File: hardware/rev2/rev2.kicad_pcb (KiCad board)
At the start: 2 copper layers, 83.8 x 94 mm, 44 parts, among them J1 Conn_01x09_Female, J2 RFM9X_header, J3 Conn_01x03_Male, Q1 Q_PNP_BCE, U1 BNO055, U2 MPL3115A2, U3 Teensy3.6, U4 BMI088, U5 ADXL345BCCZ, Y1 Crystal_32kHz768

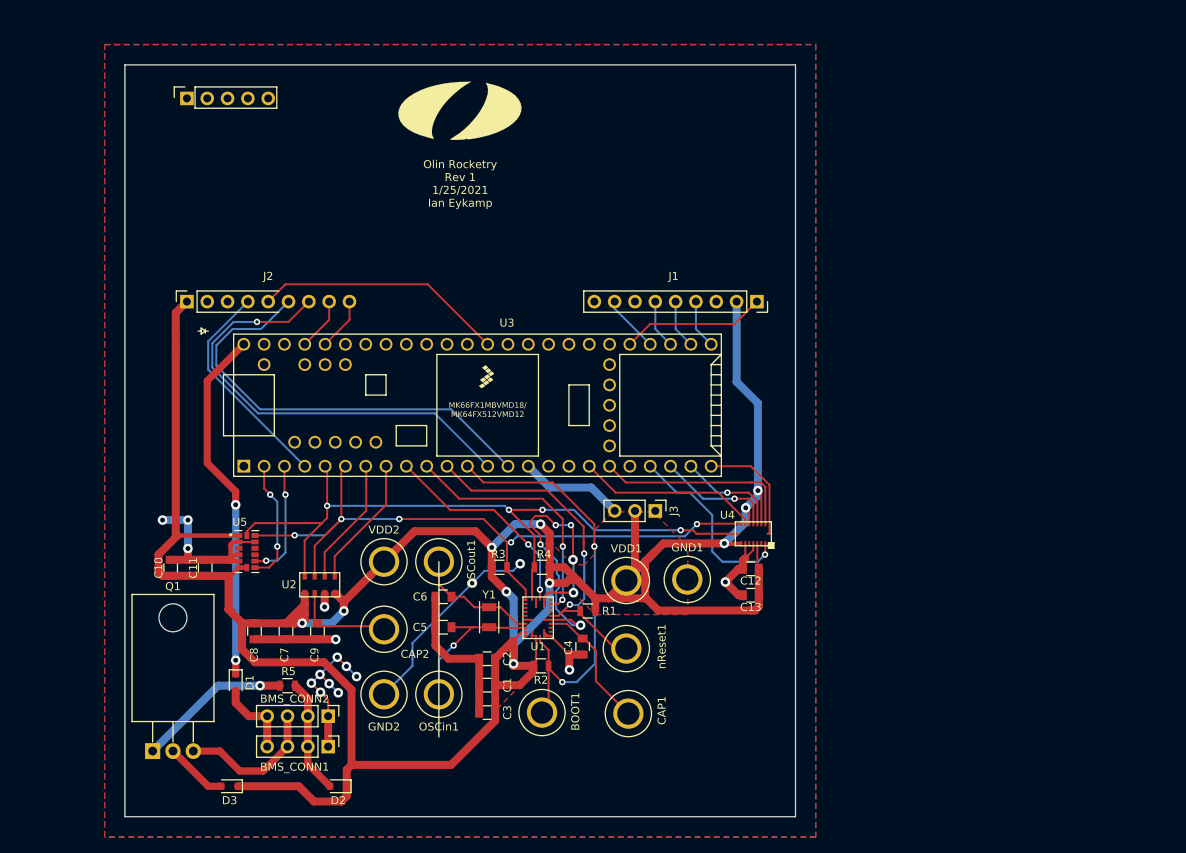
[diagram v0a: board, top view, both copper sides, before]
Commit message: remove extra traces from layout
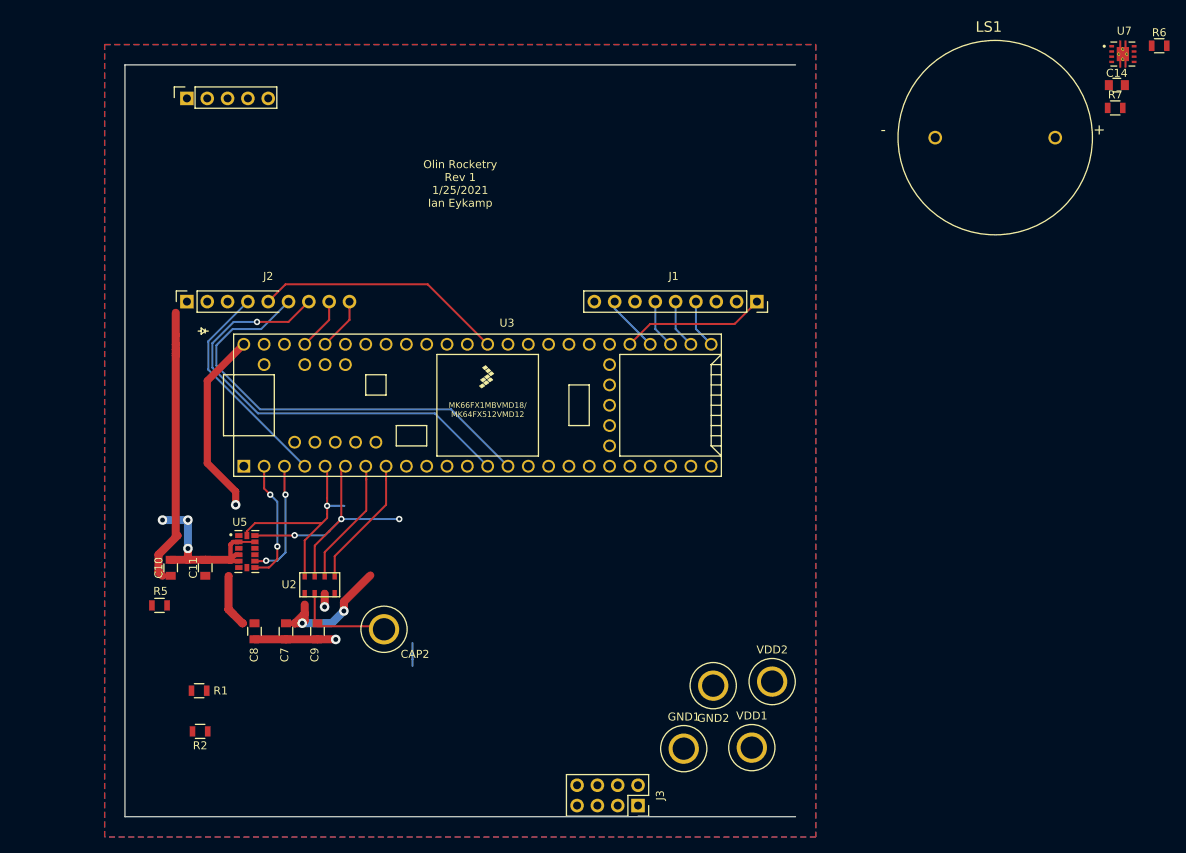
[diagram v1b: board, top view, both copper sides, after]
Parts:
- removed BMS_CONN1, BMS_CONN2: Conn_01x04_Male, Connector_PinHeader_2.54mm:PinHeader_1x04_P2.54mm_Vertical
- removed BOOT1, CAP1, OSCin1, OSCout1, nReset1: TestPoint, footprints:Test-Point-Pin_Drill2.79mm
- removed C1, C12, C13, C4: 100n, footprints:C_0805_OEM
- removed C2: 6.8n, footprints:C_0805_OEM
- removed C3: 120n, footprints:C_0805_OEM
- removed C5, C6: 22p, footprints:C_0805_OEM
- removed D1, D2, D3: D, footprints:D_0805_OEM
- removed G***: , footprints:OLIN_O
- removed Q1: Q_PNP_BCE, Package_TO_SOT_THT:TO-220-3_Horizontal_TabDown
- removed R3, R4: 10k, footprints:R_0805_OEM
- removed U1: BNO055, BNO055:BNO055
- removed U4: BMI088, footprints:bmi088
- removed Y1: Crystal_32kHz768, footprints:FC-135_3.2x1.5mm
- added C14: C_1uF, footprints:C_0805_OEM, F.Cu at (224.6, 55.0)
- added LS1: PKB24SPCH3601-B0, rev2_lib:SPKR_PKB24SPCH3601-B0, F.Cu at (209.4, 61.5)
- added R6: R_8k, footprints:R_0805_OEM, F.Cu at (229.9, 50.1)
- added R7: R_475, footprints:R_0805_OEM, F.Cu at (224.4, 57.8)
- added U7: TPS2113ADRBR, footprints:TPS2113ADRBR, F.Cu at (225.3, 51.1)
- J3: value Conn_01x03_Male -> Conn_02x03_Odd_Even; footprint Connector_PinHeader_2.54mm:PinHeader_1x03_P2.54mm_Vertical -> Connector_PinSocket_2.54mm:PinSocket_2x04_P2.54mm_Vertical
- R1, R2: value 10k -> R_4.99K
- R5: value 1K -> R_20k
- moved VDD2 50.8 mm to (181.5, 129.5)
- moved R1 49.6 mm to (109.9, 130.7)
- moved R2 43.4 mm to (110.0, 135.8)
- moved GND2 41.2 mm to (174.1, 130.0)
- moved J3 36.9 mm to (164.7, 145.0)
- moved VDD1 26.1 mm to (178.9, 137.8)
- moved GND1 21.2 mm to (170.4, 137.9)
- moved R5 18.9 mm to (104.9, 120.0)
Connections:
- C10 pad 1: 3.3VBMS -> 3.3V_TEENSY
- C11 pad 1: 3.3VBMS -> 3.3V_TEENSY
- C7 pad 1: 3.3VBMS -> 3.3V_TEENSY
- C8 pad 1: 3.3VBMS -> 3.3V_TEENSY
- J1 pad 2: 3.3VBMS -> 3.3V_TEENSY
- J2 pad 9: 3.3VBMS -> 3.3V_TEENSY
- J3 pad 1: Net-(J3-Pad1) -> GND
- J3 pad 2: 3.3VBMS -> MAIN_DEPLOY
- J3 pad 3: 3.3V_TEENSY -> 3.3VBMS
- R1 pad 1: 3.3VBMS -> 3.3V_TEENSY
- R1 pad 2: nRESET -> SCL_TEENSY
- R2 pad 1: 3.3VBMS -> 3.3V_TEENSY
- R2 pad 2: nBOOT_LOAD_PIN -> SDA_TEENSY
- R5 pad 2: BMS_to_sensors -> 3.3VBMS
- U2 pad 1: 3.3VBMS -> 3.3V_TEENSY
- U2 pad 4: 3.3VBMS -> 3.3V_TEENSY
- U3 pad 10: INT_BNO055 -> Net-(U3-Pad10)
- U3 pad 11: nRESET -> MAIN_DEPLOY
- U3 pad 12: nBOOT_LOAD_PIN -> DROGUE_DEPLOY
- U3 pad 18: A0_GYRO_BMI088 -> Net-(U3-Pad18)
- U3 pad 19: A0_ACCEL_BMI088 -> Net-(U3-Pad19)
- U3 pad 21: INT2_ACCEL_BMI088 -> BUZZER
- U3 pad 22: INT3_GYRO_BMI088 -> Net-(U3-Pad22)
- U3 pad 23: INT4_GYRO_BMI088 -> Net-(U3-Pad23)
- U3 pad 24: INT1_ACCEL_BMI088 -> Net-(U3-Pad24)
- U3 pad 45: Net-(U3-Pad45) -> SDA_TEENSY
- U3 pad 46: Net-(U3-Pad46) -> SCL_TEENSY
- U3 pad 9: COM3 -> Net-(U3-Pad9)
- U5 pad 1: 3.3VBMS -> 3.3V_TEENSY
- U5 pad 6: 3.3VBMS -> 3.3V_TEENSY
- U5 pad 7: 3.3VBMS -> 3.3V_TEENSY
- VDD1 pad 1: 3.3VBMS -> 3.3V_TEENSY
- VDD2 pad 1: 3.3VBMS -> 3.3V_TEENSY
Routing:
- net 3.3VBMS: track 370.3 -> 59.0 mm, vias 10 -> 2
- net GND: track 164.1 -> 37.8 mm, vias 23 -> 5
- net SCL_TEENSY: track 90.6 -> 27.5 mm, vias 4 -> 1
- net nBOOT_LOAD_PIN: track 54.4 -> 0.00 mm, vias 2 -> 0
- net SDA_TEENSY: track 87.3 -> 34.2 mm, vias 5 -> 3
- net nRESET: track 44.6 -> 0.00 mm, vias 2 -> 0
- net INT_BNO055: track 31.8 -> 0.00 mm, vias 2 -> 0
- net COM3: track 26.8 -> 0.00 mm, vias 2 -> 0
- net A0_ACCEL_BMI088: track 25.1 -> 0.00 mm
- net INT2_ACCEL_BMI088: track 23.7 -> 0.00 mm, vias 1 -> 0
- net A0_GYRO_BMI088: track 22.8 -> 0.00 mm
- net BMS_to_Teensy: track 44.6 -> 23.4 mm, vias 2 -> 1
- net OptionalOSCinput: track 19.8 -> 0.00 mm, vias 1 -> 0
- net Net-(R5-Pad1): track 19.3 -> 0.00 mm, vias 1 -> 0
- net BMS_to_sensors_backup: track 17.9 -> 0.00 mm
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- removed copper zone on F.Cu, net +3V3
- removed copper zone on F.Cu, net 3.3VBMS

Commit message: add DXF outline
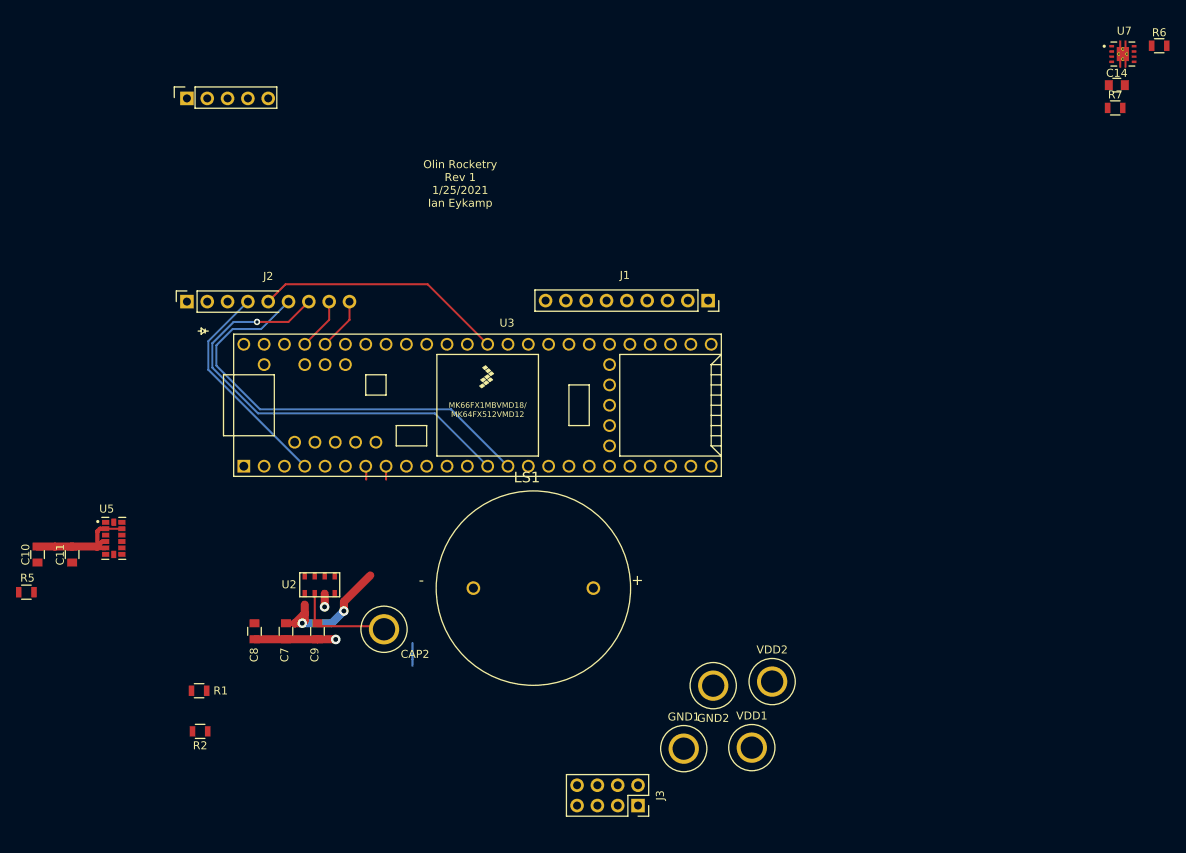
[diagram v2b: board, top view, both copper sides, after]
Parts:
- moved LS1 80.6 mm to (151.6, 117.9)
- moved C10 16.7 mm to (89.7, 113.7)
- moved C11 16.7 mm to (94.0, 113.7)
- moved R5 16.7 mm to (88.3, 118.4)
- moved U5 16.7 mm to (99.2, 111.6)
- moved J1 6.10 mm to (173.5, 81.9)
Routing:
- net 3.3VBMS: track 59.0 -> 16.8 mm
- net SDA_TEENSY: track 34.2 -> 0.00 mm, vias 3 -> 0
- net SCL_TEENSY: track 27.5 -> 0.00 mm, vias 1 -> 0
- net BMS_to_Teensy: track 23.4 -> 0.00 mm, vias 1 -> 0
- net PPS: track 18.1 -> 0.00 mm
- net INT1_ADXL345: track 15.5 -> 0.00 mm, vias 2 -> 0
- net INT2_ADXL345: track 15.1 -> 0.00 mm, vias 2 -> 0
- net INT2_MPL3115A2: track 16.7 -> 1.99 mm
- net INT1_MPL3115A2: track 15.9 -> 1.74 mm
- net GND: track 37.8 -> 29.7 mm, vias 5 -> 2
- net ENABLE_GPS: track 7.18 -> 0.00 mm
- net TX: track 6.12 -> 0.00 mm
- net RX: track 6.12 -> 0.00 mm
- net FIX: track 6.12 -> 0.00 mm
- removed copper zone on B.Cu, net GND
- removed copper zone on F.Cu, net GND
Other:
- board outline removed

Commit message: start layout
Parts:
- J3: footprint Connector_PinSocket_2.54mm:PinSocket_2x04_P2.54mm_Vertical -> Connector_PinHeader_2.54mm:PinHeader_2x03_P2.54mm_Vertical
- moved C14 124.9 mm to (116.9, 118.2)
- moved U7 124.9 mm to (117.6, 114.3)
- moved R6 124.9 mm to (122.2, 113.3)
- moved R7 124.9 mm to (116.7, 121.1)
- moved R2 54.4 mm to (157.4, 109.0), turned to 90 degrees
- moved LS1 51.5 mm to (141.7, 67.3)
- moved C10 50.1 mm to (139.7, 111.8)
- moved R1 50.0 mm to (154.9, 109.0), turned to 90 degrees
- moved C11 48.9 mm to (142.9, 111.8)
- moved U5 47.9 mm to (147.0, 109.5)
- moved R5 40.7 mm to (128.8, 122.0), turned to 270 degrees
- moved C7 39.2 mm to (158.8, 114.1)
- moved C8 39.2 mm to (154.9, 114.1)
- moved C9 39.2 mm to (162.8, 114.1)
- moved CAP2 39.2 mm to (171.1, 113.9)
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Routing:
- net SCL_TEENSY: track 0.00 -> 53.0 mm, vias 0 -> 2
- net SDA_TEENSY: track 0.00 -> 51.6 mm, vias 0 -> 2
- net ENABLE_GPS: track 0.00 -> 13.4 mm
- net 3.3VBMS: track 16.8 -> 5.18 mm, vias 2 -> 0
- net PPS: track 0.00 -> 11.1 mm
- net FIX: track 0.00 -> 11.0 mm
- net RX: track 0.00 -> 10.9 mm
- net TX: track 0.00 -> 10.9 mm
- net GND: track 29.7 -> 19.3 mm
- net INT1_MPL3115A2: track 1.74 -> 0.00 mm
- net INT2_MPL3115A2: track 1.99 -> 0.28 mm

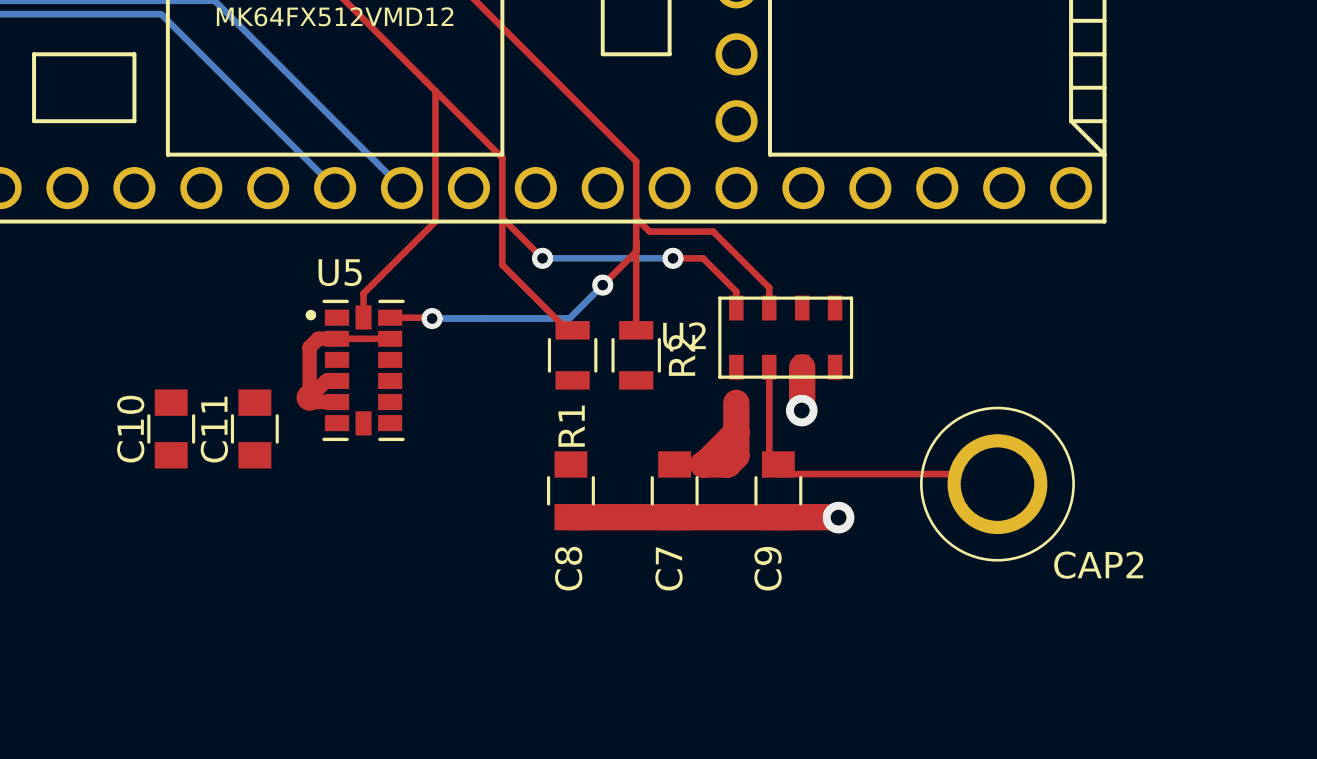
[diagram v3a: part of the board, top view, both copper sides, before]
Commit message: significantly change Teensy connections
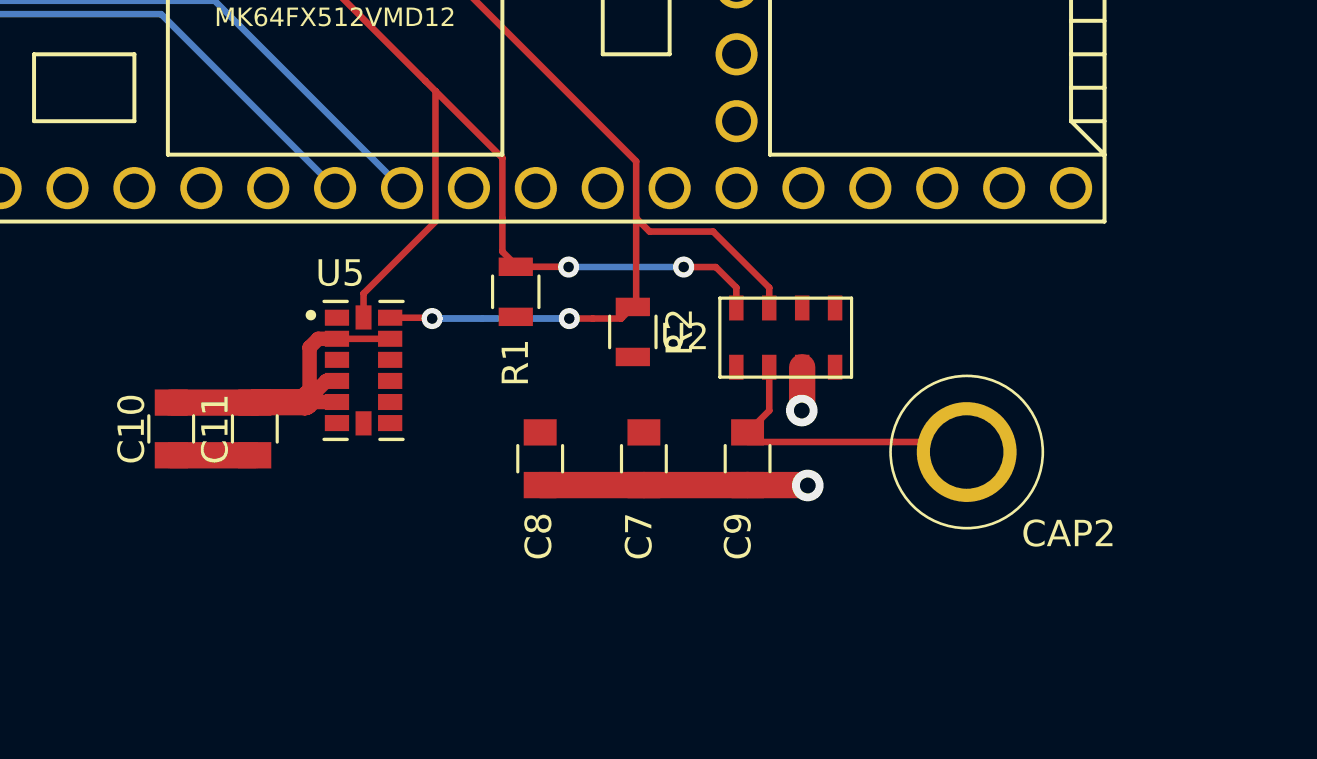
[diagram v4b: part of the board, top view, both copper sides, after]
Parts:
- moved R1 3.24 mm to (152.8, 106.6)
- moved C7 1.69 mm to (157.6, 112.9)
- moved C8 1.69 mm to (153.7, 112.9)
- moved C9 1.69 mm to (161.6, 112.9)
- moved CAP2 1.69 mm to (169.9, 112.6)
- moved R2 0.90 mm to (157.2, 108.1)
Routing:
- net GND: track 19.3 -> 24.9 mm
- net 3.3VBMS: track 5.18 -> 0.00 mm
- net SCL_TEENSY: track 53.0 -> 48.4 mm
- net 3.3V_TEENSY: track 0.00 -> 3.18 mm
- net SDA_TEENSY: track 51.6 -> 49.4 mm
- net Net-(C9-Pad1): track 12.3 -> 11.3 mm
